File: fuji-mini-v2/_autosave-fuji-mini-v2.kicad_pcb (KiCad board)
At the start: 2 copper layers, 58.4 x 81.3 mm, 58 parts, among them J1 Micro_SD_Card, J2 AudioJack3_SwitchT, J4 USB_C_Receptacle_USB2.0_14P, SW1 RotaryEncoder_Switch, U1 ESP32-S3, U2 PCM5102A, U3 TPA6110A2DGN, U4 ER_OLEDM0.91_1x-I2C, U5 MCP73831-2-MC, U6 AMS1117-3.3

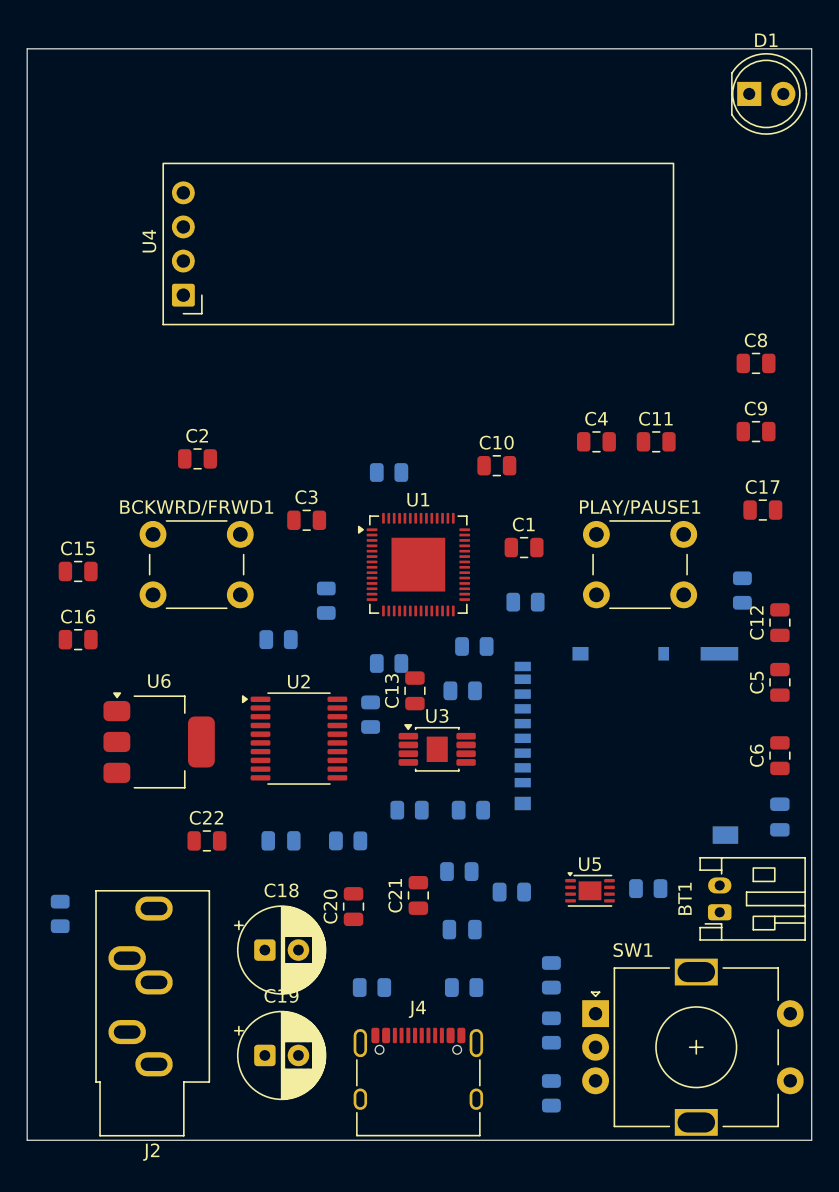
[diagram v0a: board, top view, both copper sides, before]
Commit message: Footprints + PCB v1.0
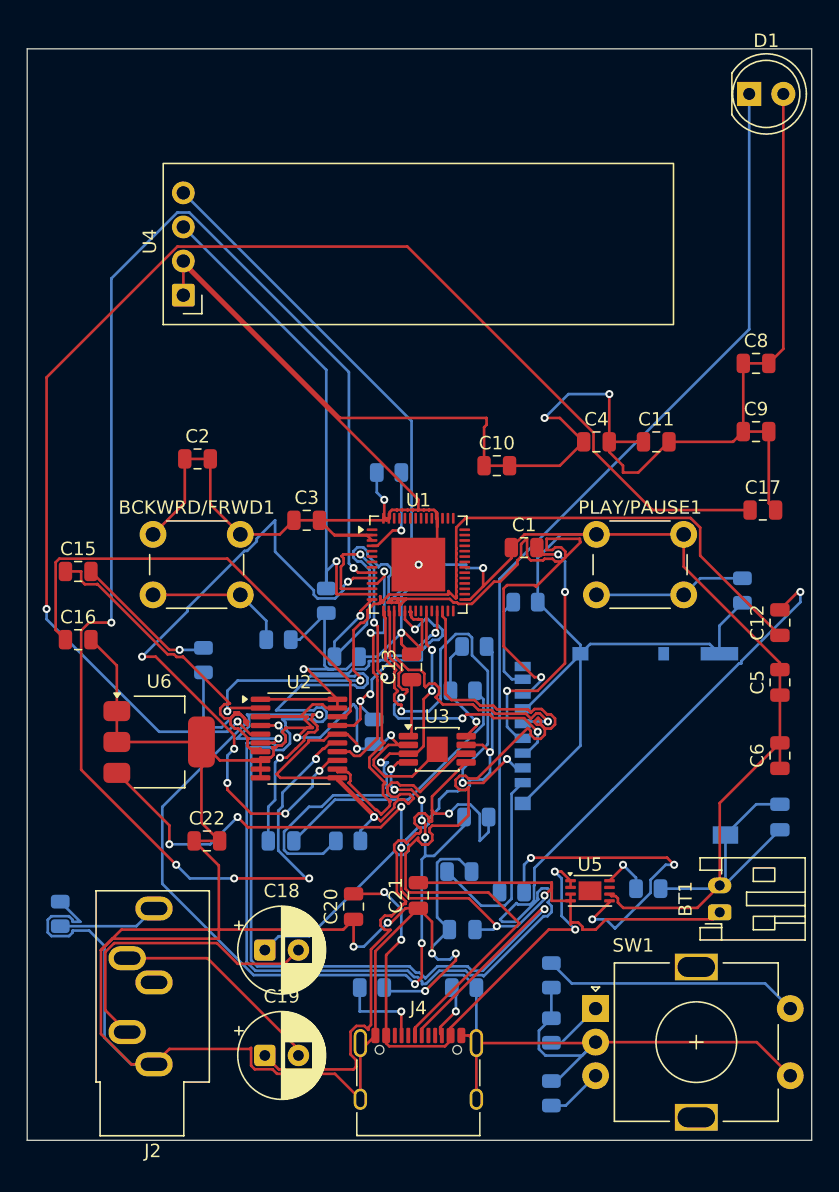
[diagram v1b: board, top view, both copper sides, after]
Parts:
- moved R5 19.0 mm to (91.9, 101.1), turned to -90 degrees
- moved R11 3.19 mm to (102.6, 100.8)
- moved C13 1.80 mm to (107.4, 101.6)
- moved R4 1.30 mm to (104.6, 106.4)
- moved R6 0.65 mm to (112.3, 112.8)
- moved SW1 0.38 mm to (121.1, 127.0)
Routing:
- net 3V3: track 0.00 -> 654.1 mm, vias 0 -> 16
- net I2S_LRCK: track 0.00 -> 113.1 mm, vias 0 -> 6
- net Net-(U2-VNEG): track 0.00 -> 103.5 mm, vias 0 -> 2
- net USB_DN: track 0.00 -> 92.7 mm, vias 0 -> 2
- net Net-(U2-CAPM): track 0.00 -> 92.0 mm, vias 0 -> 2
- net VBAT: track 0.00 -> 75.0 mm, vias 0 -> 6
- net Net-(U3-IN2-): track 0.00 -> 68.5 mm, vias 0 -> 7
- net Net-(D1-K): track 0.00 -> 67.1 mm
- net Net-(U2-CAPP): track 0.00 -> 63.7 mm, vias 0 -> 2
- net USB_DP: track 0.00 -> 63.4 mm
- net I2C_SDA: track 0.00 -> 59.9 mm, vias 0 -> 1
- net I2S_BCK: track 0.00 -> 50.9 mm, vias 0 -> 6
- net VO2: track 0.00 -> 47.8 mm, vias 0 -> 1
- net GPIO13: track 0.00 -> 44.7 mm, vias 0 -> 1
- net VDD: track 0.00 -> 39.8 mm, vias 0 -> 4
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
